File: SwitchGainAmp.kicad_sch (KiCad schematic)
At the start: 22 parts, among them Q3 BSS138, Q4 BSS138, Q5 BSS138, Q6 BSS138, U8 LT1493

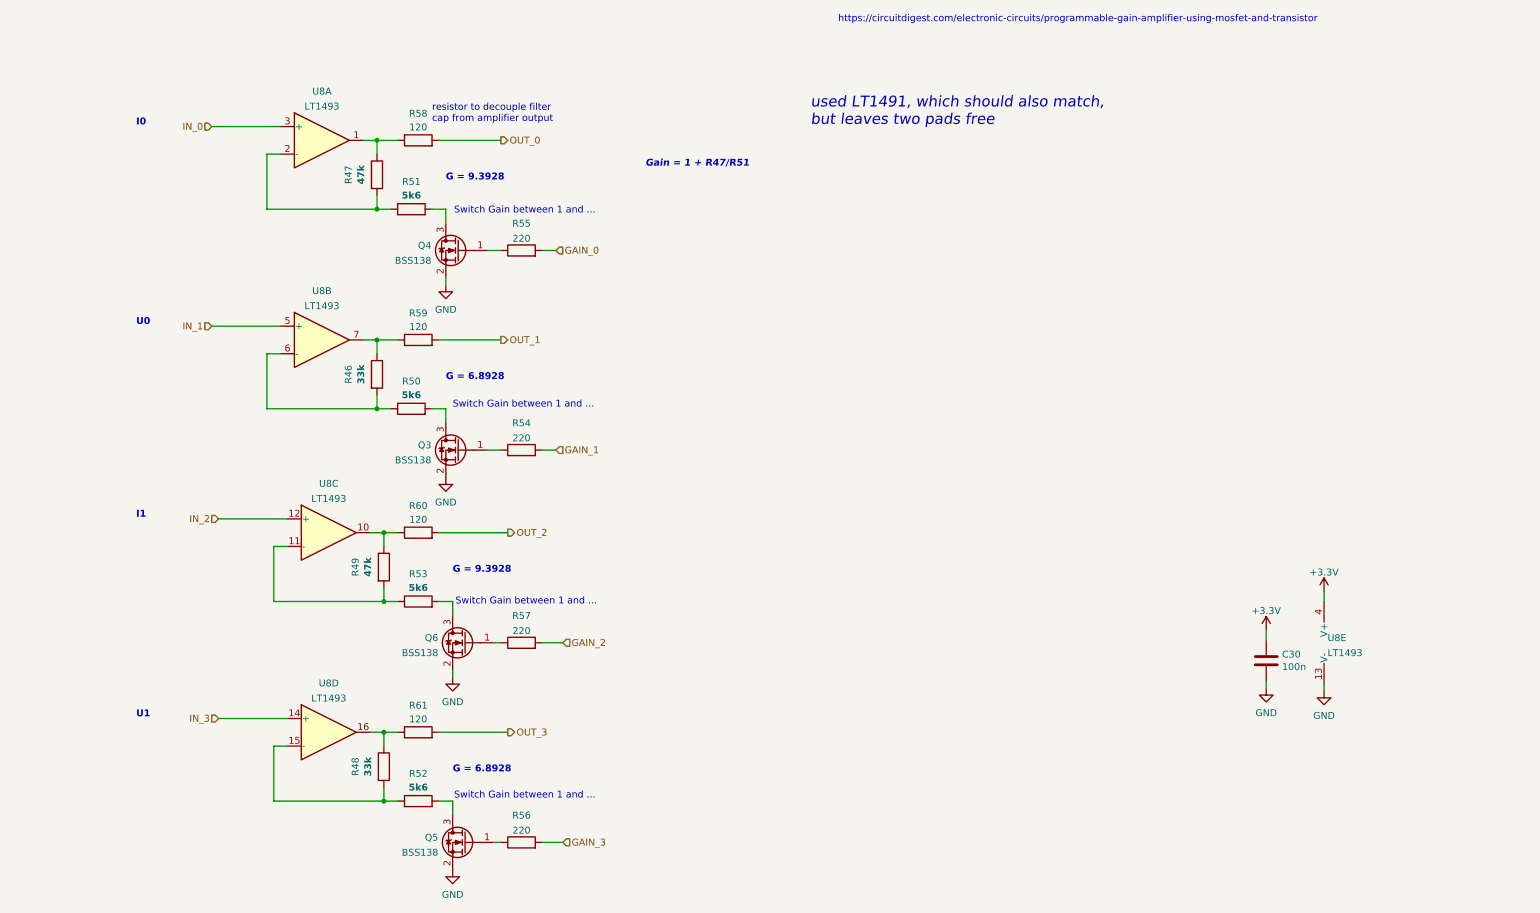
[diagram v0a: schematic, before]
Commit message: changed U8 to LT1491
get some space on the PCB by removing the non needed pads
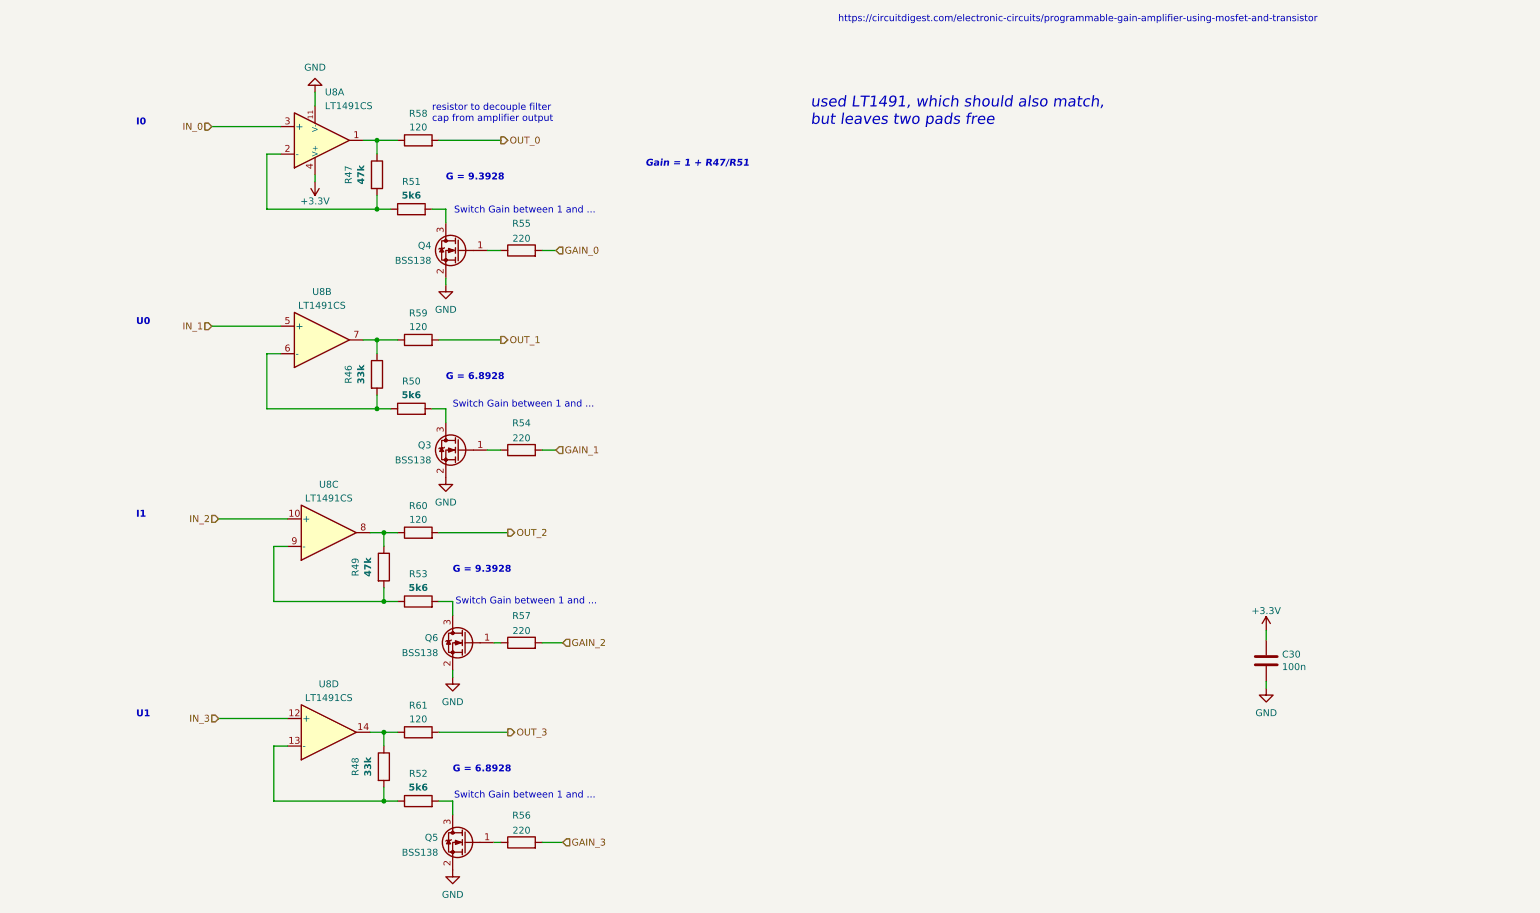
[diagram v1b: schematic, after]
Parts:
- removed U8: LT1493, Package_SO:SOIC-16_3.9x9.9mm_P1.27mm, symbol Amplifier_Operational:LT1493
- added U8: LT1491CS, Package_SO:SOIC-14_3.9x8.7mm_P1.27mm, symbol PCM_Amplifier_Operational_AKL:LT1491CS
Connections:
- net +3.3V: now also U8.4 (V+)
- net GND: now also U8.11 (V-)
- net IN_0: now also U8.3 (+)
- net IN_1: now also U8.5 (+)
- net IN_2: now also U8.10 (+)
- net IN_3: now also U8.12 (+)
- net at R49.2, R53.1: now also U8.9 (-)
- net at R47.1, R58.1: now also U8.1
- net at R46.2, R50.1: now also U8.6 (-)
- net at R48.1, R61.1: now also U8.14
- net at R47.2, R51.1: now also U8.2 (-)
- net at R46.1, R59.1: now also U8.7
- net at R49.1, R60.1: now also U8.8
- net at R48.2, R52.1: now also U8.13 (-)

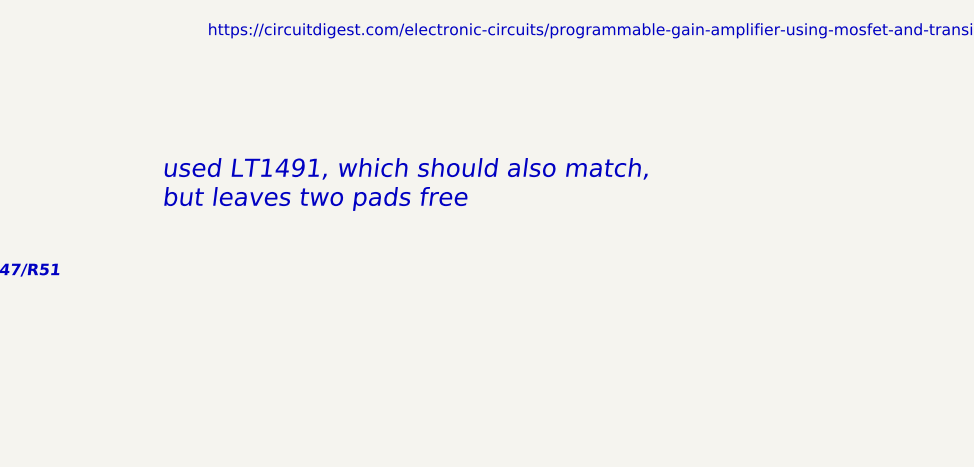
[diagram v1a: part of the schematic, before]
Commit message: removed comment about LT1491
because LT1491 is used.
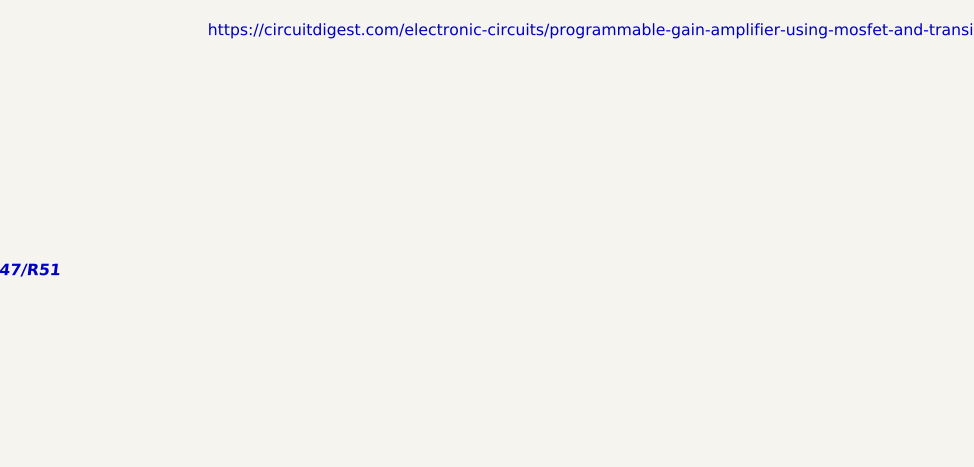
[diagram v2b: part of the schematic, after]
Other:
- note removed: "used LT1491, which should also match, but leaves two pads free"
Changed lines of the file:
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@@
     (effects (font (size 1.27 1.27)) (justify left bottom))
-  )
-  (text "used LT1491, which should also match, \nbut leaves two pads free"
-    (at 172.72 36.83 0)
-    (effects (font (size 2 2) italic) (justify left bottom))
   )
   (text "G = 9.3928" (at 105.41 46.99 0)

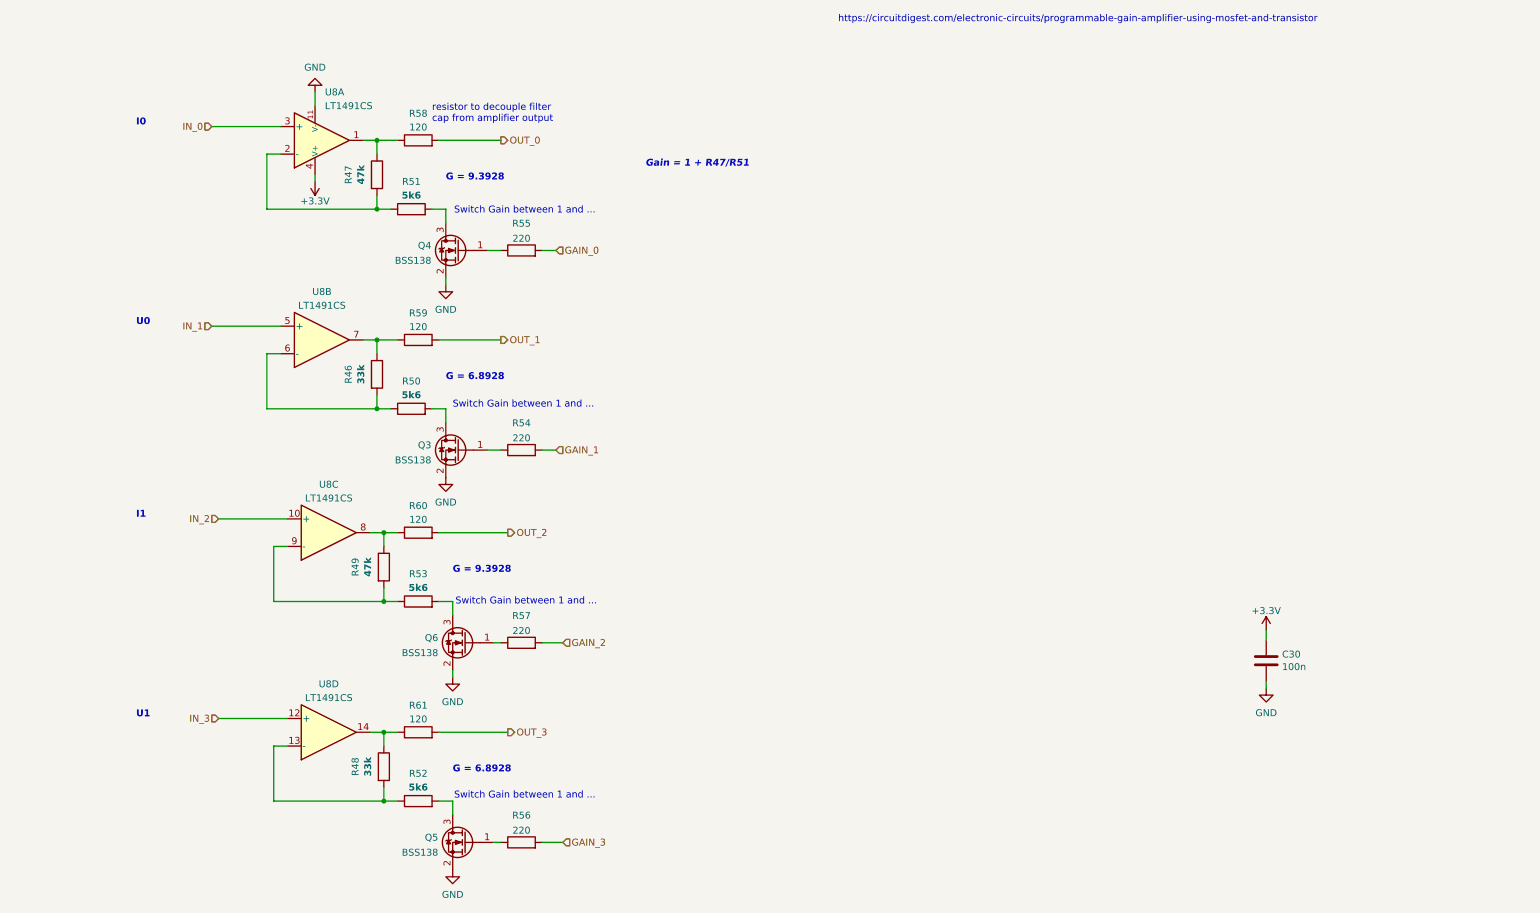
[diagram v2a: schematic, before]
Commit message: changed gain switch to CD4066
this analog switch allows usage of a bias voltage
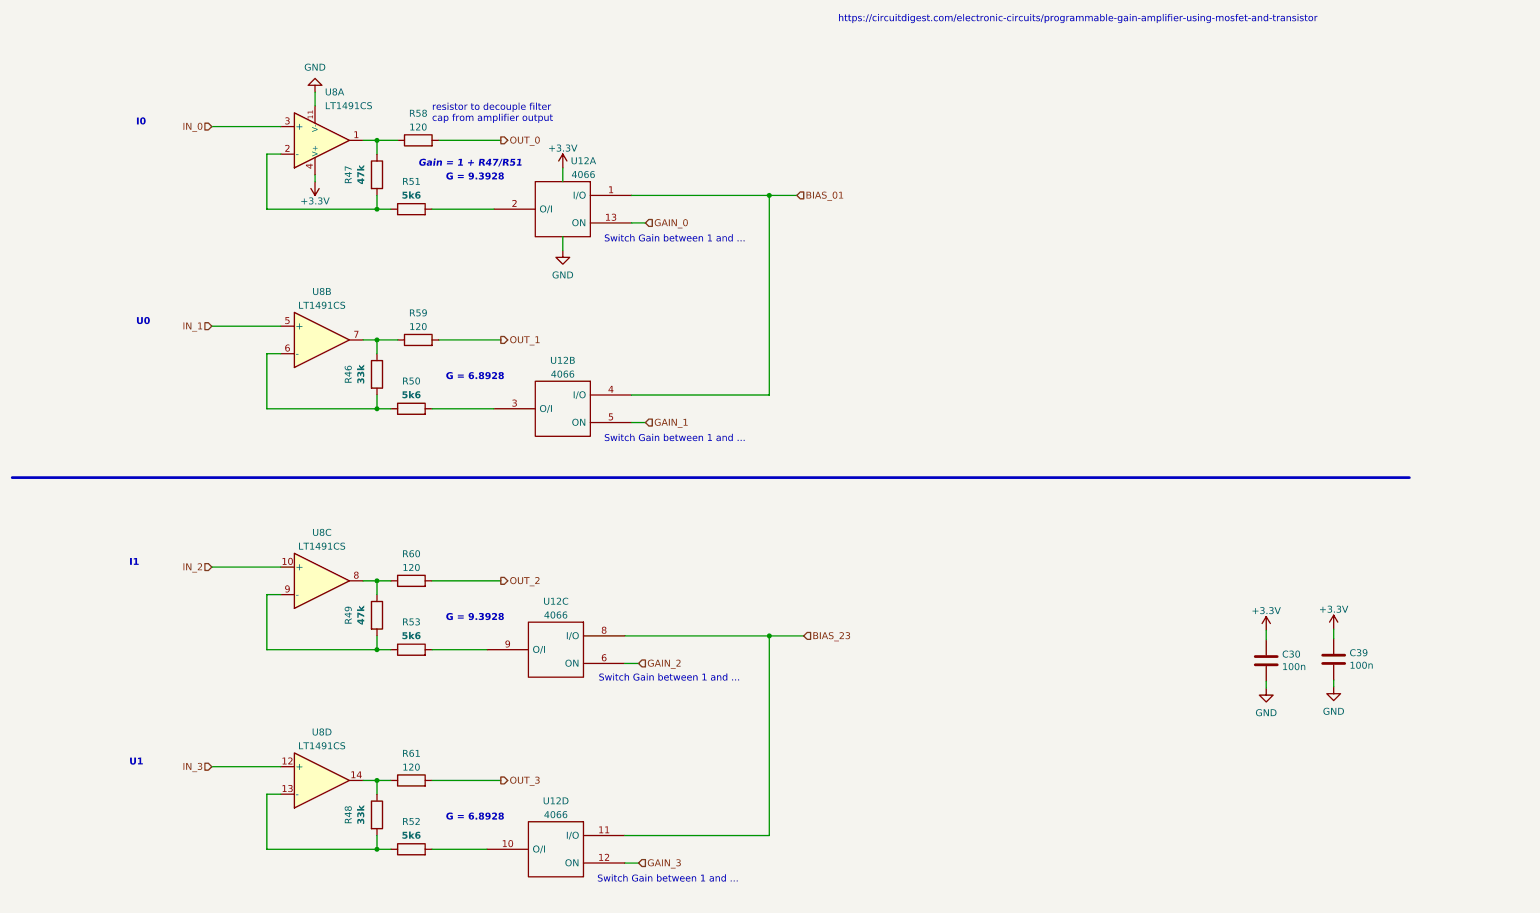
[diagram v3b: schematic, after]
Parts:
- removed Q3, Q4, Q5, Q6: BSS138, Package_TO_SOT_SMD:SOT-23, symbol Transistor_FET:BSS138
- removed R54, R55, R56, R57: 220, Resistor_SMD:R_0603_1608Metric, symbol Device:R
- added C39: 100n, Capacitor_SMD:C_0603_1608Metric, symbol Device:C
- added U12: 4066, Package_SO:SOIC-14_3.9x8.7mm_P1.27mm, symbol 4xxx_IEEE:4066
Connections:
- net +3.3V: now also C39.1, U12.14 (Vdd), U12.14 (Vdd), U12.14 (Vdd), U12.14 (Vdd)
- net GAIN_0: now also U12.13 (ON)
- net GAIN_1: now also U12.5 (ON)
- net GAIN_2: now also U12.6 (ON)
- net GAIN_3: now also U12.12 (ON)
- net GND: now also C39.2, U12.7 (Vss), U12.7 (Vss), U12.7 (Vss), U12.7 (Vss)
- net at R53.2: now also U12.9 (O/I)
- net at R51.2: now also U12.2 (O/I)
- net at R50.2: now also U12.3 (O/I)
- net at R52.2: now also U12.10 (O/I)
- new net BIAS_01: U12.1 (I/O), U12.4 (I/O)
- new net BIAS_23: U12.11 (I/O), U12.8 (I/O)
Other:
- moved on the sheet: R48, R49, R52, R53, R60, R61, U8C, U8D
